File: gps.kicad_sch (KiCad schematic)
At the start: 9 parts, among them J6 Conn_Coaxial, U1 NEO-M9N-00B

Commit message: Remove non-existent security fields from bluer characteristics
The bluer crate's CharacteristicWrite and CharacteristicNotify
don't have encrypt_*/secure_* fields - removed them.

Co-Authored-By: Claude Opus 4.5 <noreply@anthropic.com>
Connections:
- net +3V3 renamed +3.3V
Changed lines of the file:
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@@
 			)
 		)
-		(property "Value" "+3V3"
+		(property "Value" "+3.3V"
 			(at 87.1156 79.6417 0)
 			(effects
@@
 			)
 		)
-		(property "Value" "+3V3"
+		(property "Value" "+3.3V"
 			(at 199.9044 82.9183 0)
 			(effects
@@
 			)
 		)
-		(property "Value" "+3V3"
+		(property "Value" "+3.3V"
 			(at 87.1156 94.8817 0)
 			(effects

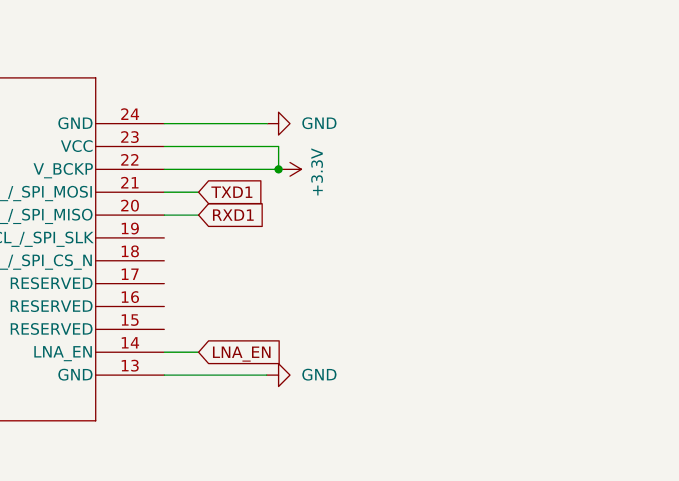
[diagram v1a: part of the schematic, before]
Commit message: Rename project to Perfect-Vision-ECU
- Rename main project files from Raspberry-Pi-Backup-power-and-GPS-hat-v4
- Update relay footprint to G6K-2F-Y to match LCSC part C397194
- Update C4 capacitor to CP_Elec_8x10.5 with LCSC C3353 (220uF 25V)
- Add new power supply schematic
- Update JLCPCB production files (gerbers, BOM, CPL)
- Remove old firmware and Raspberry Pi specific files

Co-Authored-By: Claude Opus 4.5 <noreply@anthropic.com>
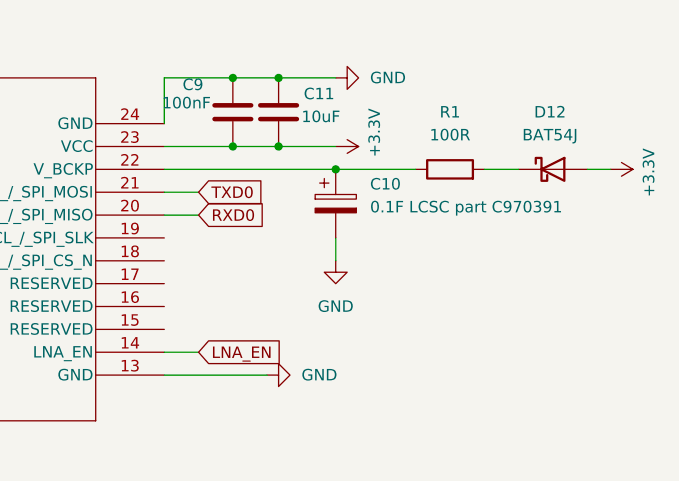
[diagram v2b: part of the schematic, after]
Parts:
- added C10: 0.1F LCSC part C970391, Capacitor_THT:CP_Radial_D8.0mm_P3.50mm, symbol Device:C_Polarized
- added C11: 10uF, Capacitor_SMD:C_0805_2012Metric, symbol Device:C
- added C9: 100nF, Capacitor_SMD:C_0402_1005Metric, symbol Device:C
- added D12: BAT54J, Diode_SMD:D_SOD-323F, symbol Diode:BAT54J
- added R1: 100R, Resistor_SMD:R_0402_1005Metric, symbol Device:R
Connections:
- net +3.3V: now also C11.2, C9.2, D12.2 (A); no longer U1.22 (V_BCKP)
- net GND: now also C10.2, C11.1, C9.1
- net RXD1 renamed RXD0
- net TXD1 renamed TXD0
- new net: D12.1 (K), R1.2
- new net: C10.1, R1.1, U1.22 (V_BCKP)
